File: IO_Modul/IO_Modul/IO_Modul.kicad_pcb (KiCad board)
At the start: 4 copper layers, 105 x 100 mm, 76 parts, among them J101 Conn_02x20_Odd_Even, J102 Screw_Terminal_01x02, J103 Screw_Terminal_01x02, J104 Screw_Terminal_01x02, J105 Screw_Terminal_01x02, J106 Screw_Terminal_01x02, J107 Screw_Terminal_01x02, J108 Screw_Terminal_01x02, J109 Screw_Terminal_01x02, J110 Screw_Terminal_01x02, J111 Screw_Terminal_01x02, J112 Screw_Terminal_01x02, J113 Screw_Terminal_01x02, J114 Screw_Terminal_01x02, J115 Screw_Terminal_01x02, J116 Screw_Terminal_01x02, J117 Screw_Terminal_01x02, J118 Screw_Terminal_01x02, J119 Screw_Terminal_01x02, J120 Screw_Terminal_01x02, J121 Screw_Terminal_01x02, J122 Screw_Terminal_01x02, Q101 Si4431CDY, Q102 Si4431CDY, Q103 Si4431CDY, Q104 Si4431CDY, Q105 Si4431CDY, Q106 2N7002, Q107 2N7002, Q108 2N7002, Q109 2N7002, Q110 2N7002, Q111 Si4431CDY, Q112 Si4431CDY, Q113 Si4431CDY, Q114 Si4431CDY, Q115 Si4431CDY, Q116 2N7002, Q117 2N7002, Q118 2N7002, Q119 2N7002, Q120 2N7002

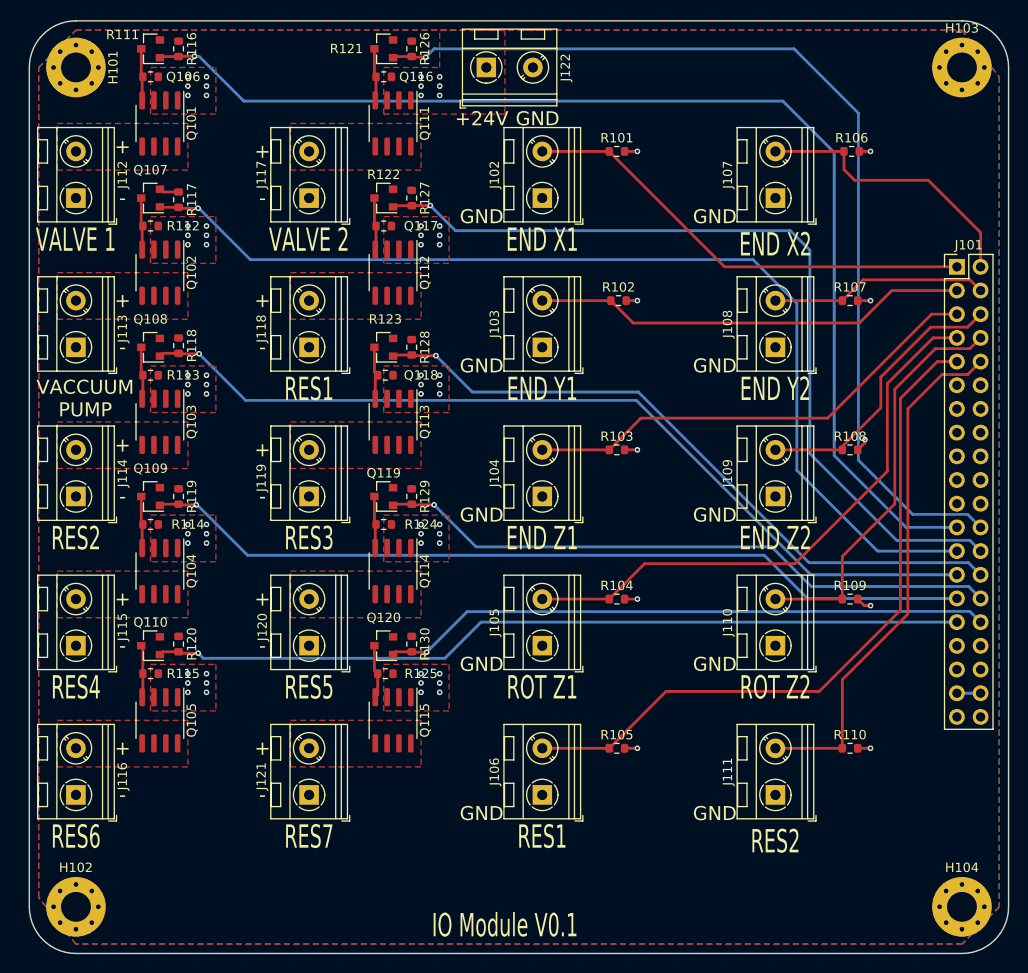
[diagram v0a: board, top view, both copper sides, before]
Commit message: Feeder Microswitch für Tape Motor hinzugefügt. Einige 3D Step Modelle hinzugefügt. Stepper Board die Ecken abgerundet.
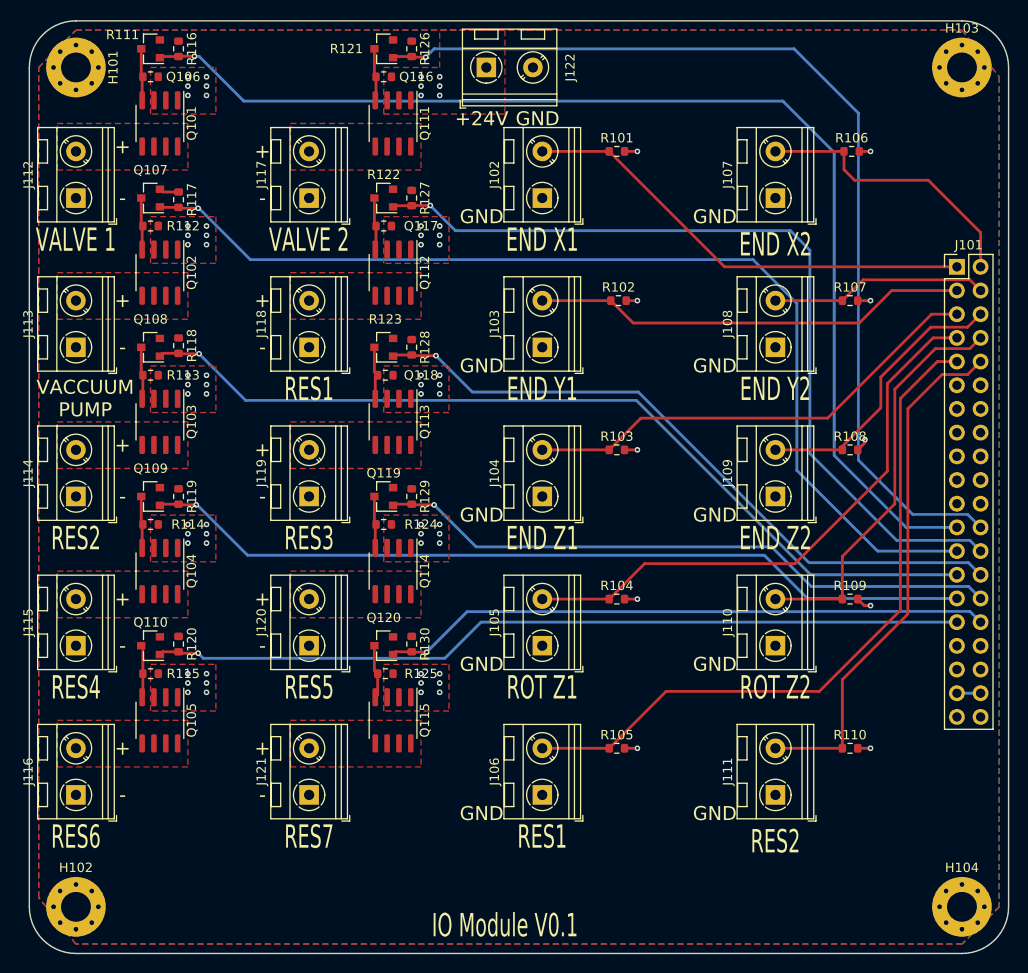
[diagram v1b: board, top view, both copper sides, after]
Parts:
- J102, J103, J104, J105, J106, J107, J108, J109, J110, J111, J112, J113, J114, J115, J116, J117, J118, J119, J120, J121, J122: footprint TerminalBlock_RND:TerminalBlock_RND_205-00045_1x02_P5.00mm_Horizontal -> ProjectFootprints:TerminalBlock_RND_205-00045_1x02_P5.00mm_Horizontal

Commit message: Fiducials auf allen Boards hinzugefügt
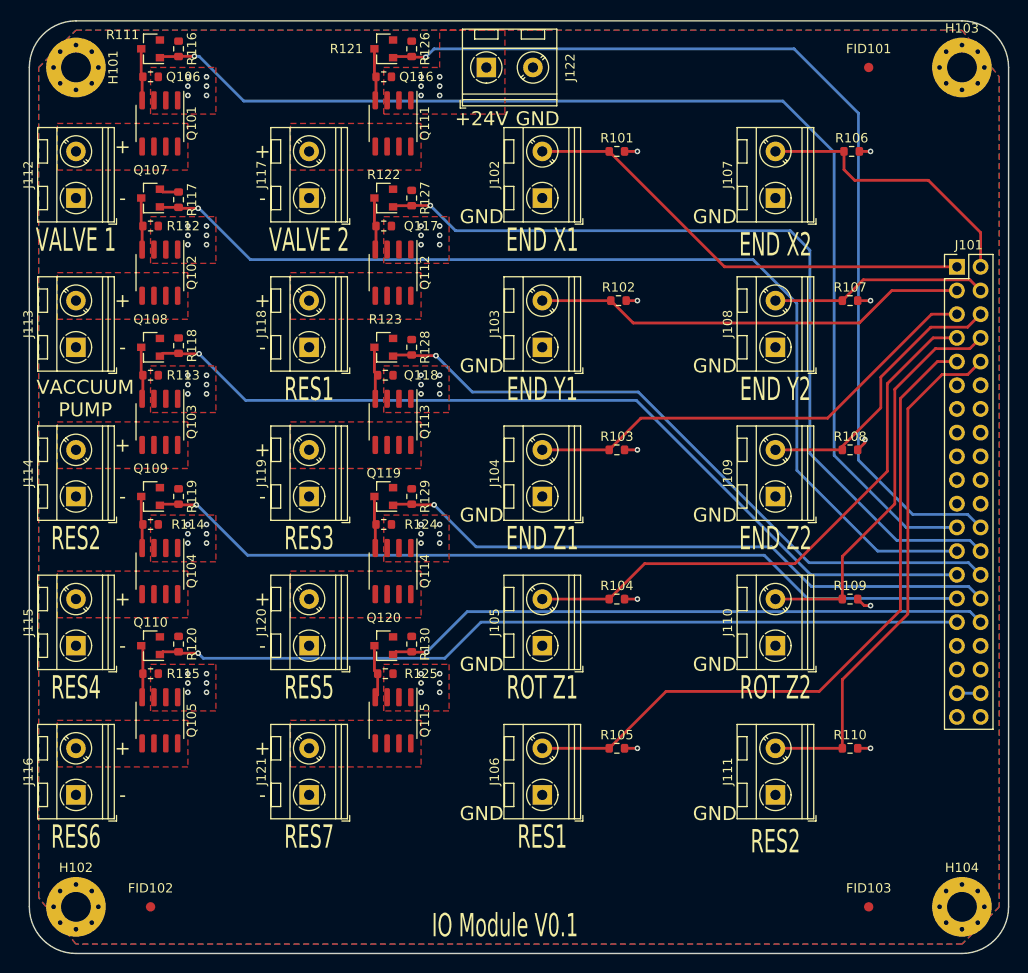
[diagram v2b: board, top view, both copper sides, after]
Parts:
- added FID101: Fiducial, Fiducial:Fiducial_1mm_Mask2mm, F.Cu at (120.0, 55.0)
- added FID102: Fiducial, Fiducial:Fiducial_1mm_Mask2mm, F.Cu at (43.0, 145.0)
- added FID103: Fiducial, Fiducial:Fiducial_1mm_Mask2mm, F.Cu at (120.0, 145.0)

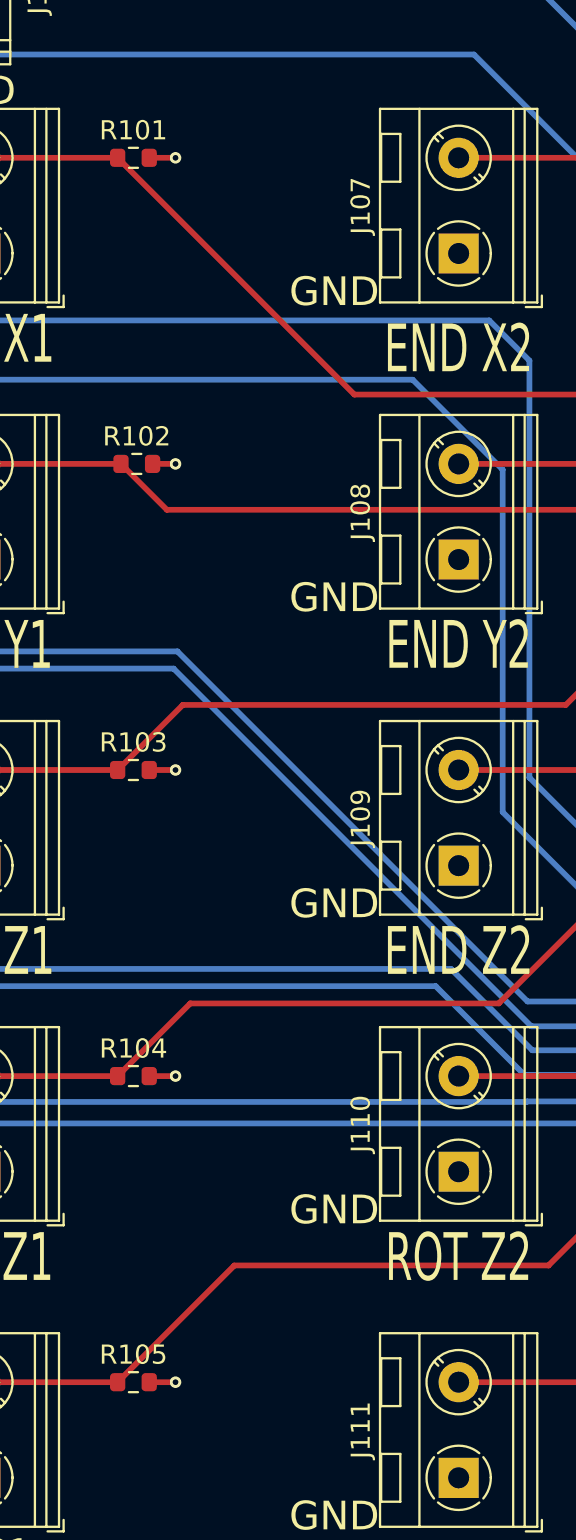
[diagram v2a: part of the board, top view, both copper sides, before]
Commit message: ESD Protection überarbeitet, aber noch nicht fertig
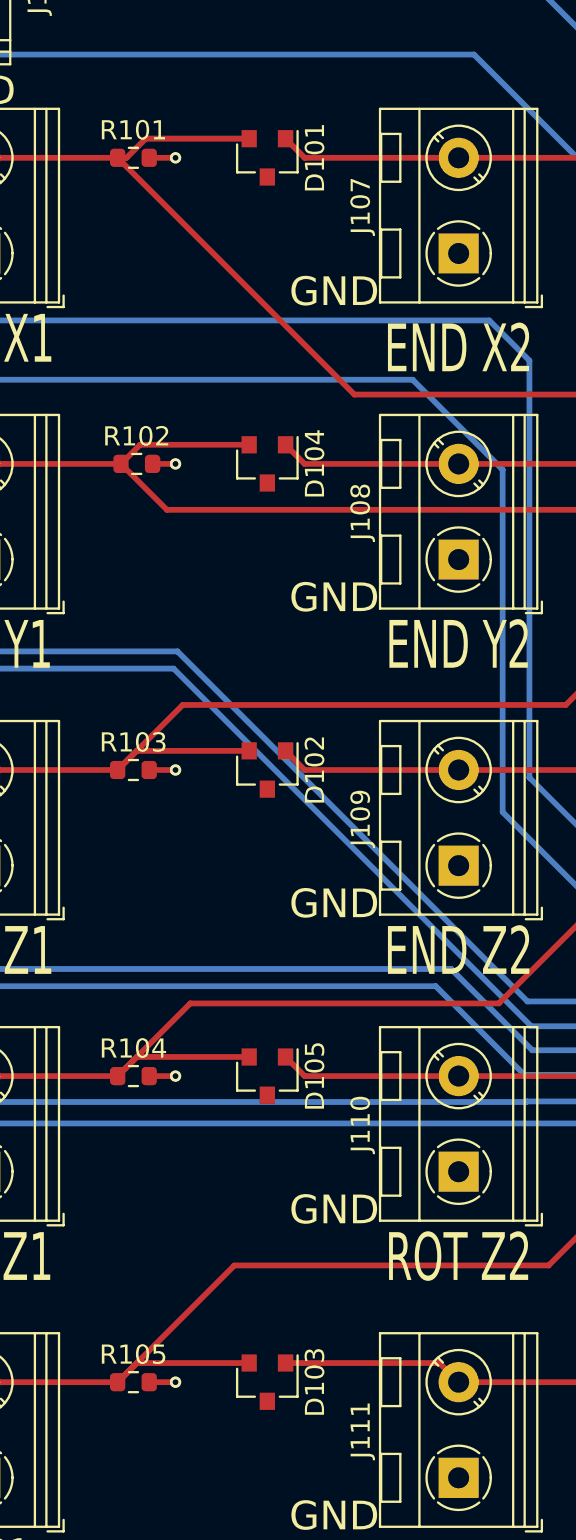
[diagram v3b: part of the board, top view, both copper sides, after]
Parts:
- added D101: MMBZ9V1AL-7-F, Package_TO_SOT_SMD:SOT-23, F.Cu at (100.0, 64.0)
- added D102: MMBZ9V1AL-7-F, Package_TO_SOT_SMD:SOT-23, F.Cu at (100.0, 96.0)
- added D103: MMBZ9V1AL-7-F, Package_TO_SOT_SMD:SOT-23, F.Cu at (100.0, 128.0)
- added D104: MMBZ9V1AL-7-F, Package_TO_SOT_SMD:SOT-23, F.Cu at (100.0, 80.0)
- added D105: MMBZ9V1AL-7-F, Package_TO_SOT_SMD:SOT-23, F.Cu at (100.0, 112.0)
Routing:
- net /ENDSTOP_X2: track 30.4 -> 39.9 mm
- net /ENDSTOP_Y2: track 23.4 -> 32.9 mm
- net /ENDSTOP_Z2: track 30.2 -> 39.6 mm
- net /ENDSTOP_ROT2: track 43.5 -> 52.9 mm
- net /INPUT_RES2: track 56.4 -> 65.8 mm
- net /INPUT_RES1: track 74.9 -> 82.2 mm
- net /ENDSTOP_X1: track 49.6 -> 56.9 mm
- net /ENDSTEP_Z1: track 50.5 -> 57.8 mm
- net /ENDSTOP_Y1: track 46.9 -> 54.0 mm
- net /ENDSTOP_ROT1: track 61.6 -> 68.3 mm

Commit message: Änderungen für bestellung V01 -  Bestellung abgeschickt
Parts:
- added D106: MMBZ9V1AL-7-F, Package_TO_SOT_SMD:SOT-23, F.Cu at (101.2, 138.7)
- added D107: MMBZ9V1AL-7-F, Package_TO_SOT_SMD:SOT-23, F.Cu at (69.8, 136.9)
- added J123: Screw_Terminal_01x03, TerminalBlock_RND:TerminalBlock_RND_205-00046_1x03_P5.00mm_Horizontal, F.Cu at (65.5, 145.5)
- added J124: Screw_Terminal_01x03, TerminalBlock_RND:TerminalBlock_RND_205-00046_1x03_P5.00mm_Horizontal, F.Cu at (82.0, 145.5)
- added J125: Screw_Terminal_01x03, TerminalBlock_RND:TerminalBlock_RND_205-00046_1x03_P5.00mm_Horizontal, F.Cu at (98.5, 145.5)
- added J126: Screw_Terminal_01x03, TerminalBlock_RND:TerminalBlock_RND_205-00046_1x03_P5.00mm_Horizontal, F.Cu at (115.0, 145.5)
- moved FID102 5.00 mm to (48.0, 145.0)
- moved H101 5.00 mm to (40.0, 55.0)
- moved H102 5.00 mm to (40.0, 145.0)
- moved J112 4.50 mm to (39.5, 69.0)
- moved J113 4.50 mm to (39.5, 85.0)
- moved J114 4.50 mm to (39.5, 101.0)
- moved J115 4.50 mm to (39.5, 117.0)
- moved J116 4.50 mm to (39.5, 133.0)
- moved Q101 4.00 mm to (48.0, 61.0)
- moved Q102 4.00 mm to (48.0, 77.0)
- moved Q103 4.00 mm to (48.0, 93.0)
- moved Q104 4.00 mm to (48.0, 109.0)
- moved Q105 4.00 mm to (48.0, 125.0)
- moved Q106 4.00 mm to (47.0, 53.0)
- moved Q107 4.00 mm to (47.0, 69.0)
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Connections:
- J101 pad 15: (no net) -> /ADC_RES1
- J101 pad 16: (no net) -> /ADC_RES2
- J101 pad 17: (no net) -> /ADC_RES3
- J101 pad 18: (no net) -> /ADC_RES4
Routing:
- net /ADC_RES1: track 0.00 -> 114.4 mm
- net /ADC_RES2: track 0.00 -> 109.4 mm
- net /ADC_RES3: track 0.00 -> 78.4 mm
- net +3V3: track 181.8 -> 258.2 mm
- net /ADC_RES4: track 0.00 -> 74.4 mm
- net /OUTPUT_RES2: track 95.4 -> 91.4 mm
- net /OUTPUT_RES4: track 89.7 -> 85.7 mm
- net /OUTPUT_RES6: track 87.5 -> 83.5 mm
- net /VENTIL2: track 106.5 -> 103.5 mm
- net /OUTPUT_RES3: track 72.8 -> 69.8 mm
- net /OUTPUT_RES1: track 91.2 -> 88.2 mm
- net /OUTPUT_RES7: track 65.4 -> 62.4 mm
- net /OUTPUT_RES5: track 67.2 -> 64.3 mm
- net GND: track 2.12 -> 0.00 mm
- net /VENTIL1: track 125.5 -> 123.4 mm
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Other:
- board size 105 x 100 mm -> 100 x 100 mm
- board text added: "3V3"
- board text added: "ADC1"
- board text added: "ADC2"
- board text added: "ADC3"
- board text added: "ADC4"
